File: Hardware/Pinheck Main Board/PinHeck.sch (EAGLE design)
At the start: 494 parts, among them IC2 PIC32MX795F512L-80I/PT, IC3 CD74HCT244E, IC4 CD74HCT244E, IC5 ULN2803A, J1 N/A, U1 P8X32A-Q44, U10 74HCT2G04GV,125, U11 74HC165D-Q100,118, U12 74HC165D-Q100,118, U13 CAT24M01LI-G, U14 MC74HC08ADR2G, U15 MC74HC08ADR2G, U16 MC74HC08ADR2G, U17 MC74HC08ADR2G, U18 MC74HC08ADR2G, U19 MC74HC08ADR2G, U2 DS1340Z-33+, U20 TIP107, U21 TIP107, U22 TIP107, U23 TIP107, U24 TIP107, U25 TIP107, U26 TIP107, U27 TIP107, U28 TIP102, U29 TIP102, U3 CD74HC595M96, U30 TIP102, U31 TIP102, U32 TIP102, U33 TIP102, U34 TIP102, U35 TIP102, U36 WS2801, U38 WS2801, U39 NCP1117DT33G, U4 CAT24M01LI-G, U5 CD74HC595M96, U52 CD74HC123M96, U6 TPS259251, U7 TPS259261, X1 FQ7050B-8.000, X2 9C-6.500MAAJ-T, X3 ABS25-32.768KHz-1-T

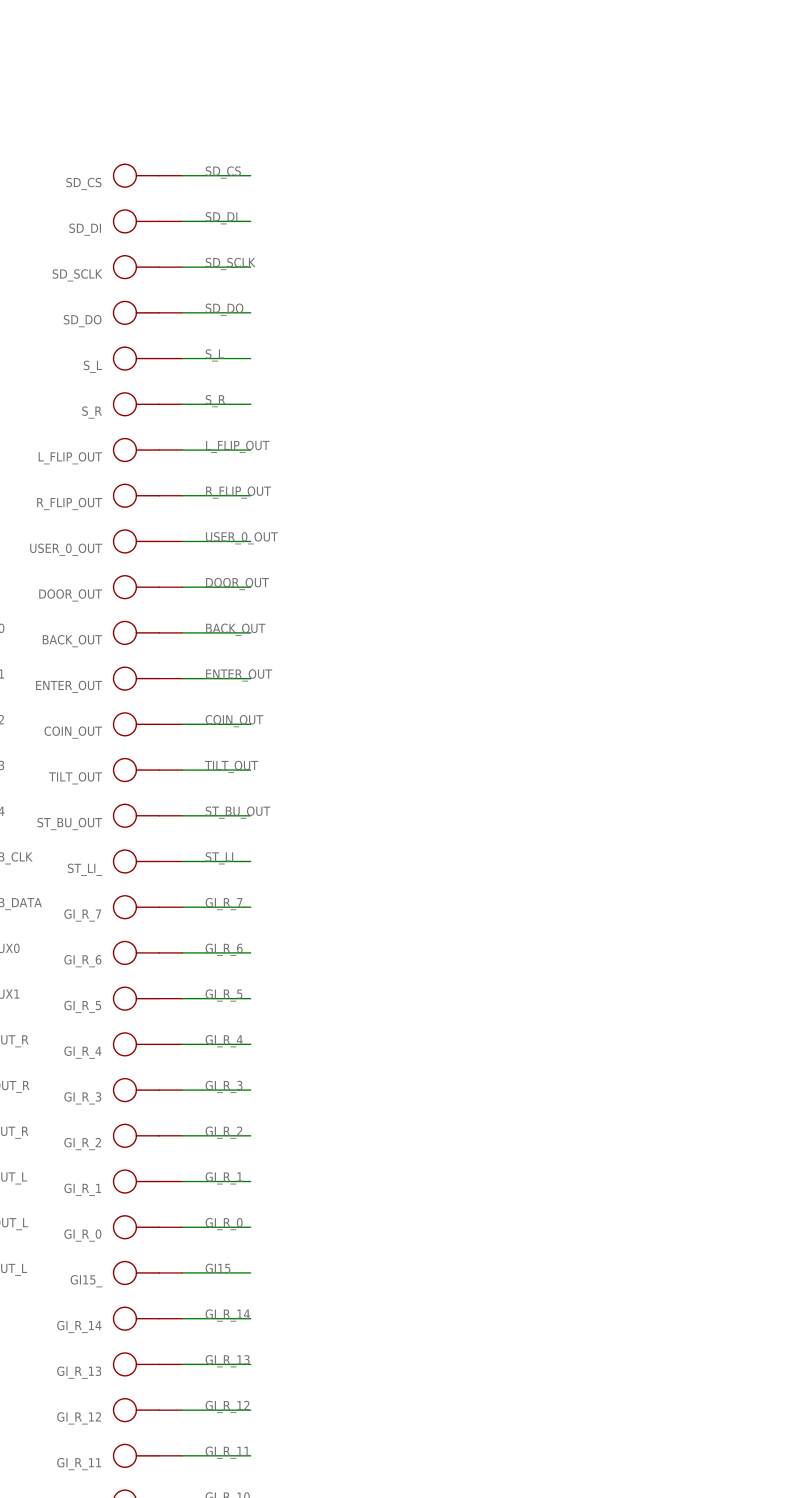
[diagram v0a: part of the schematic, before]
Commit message: finished test points.
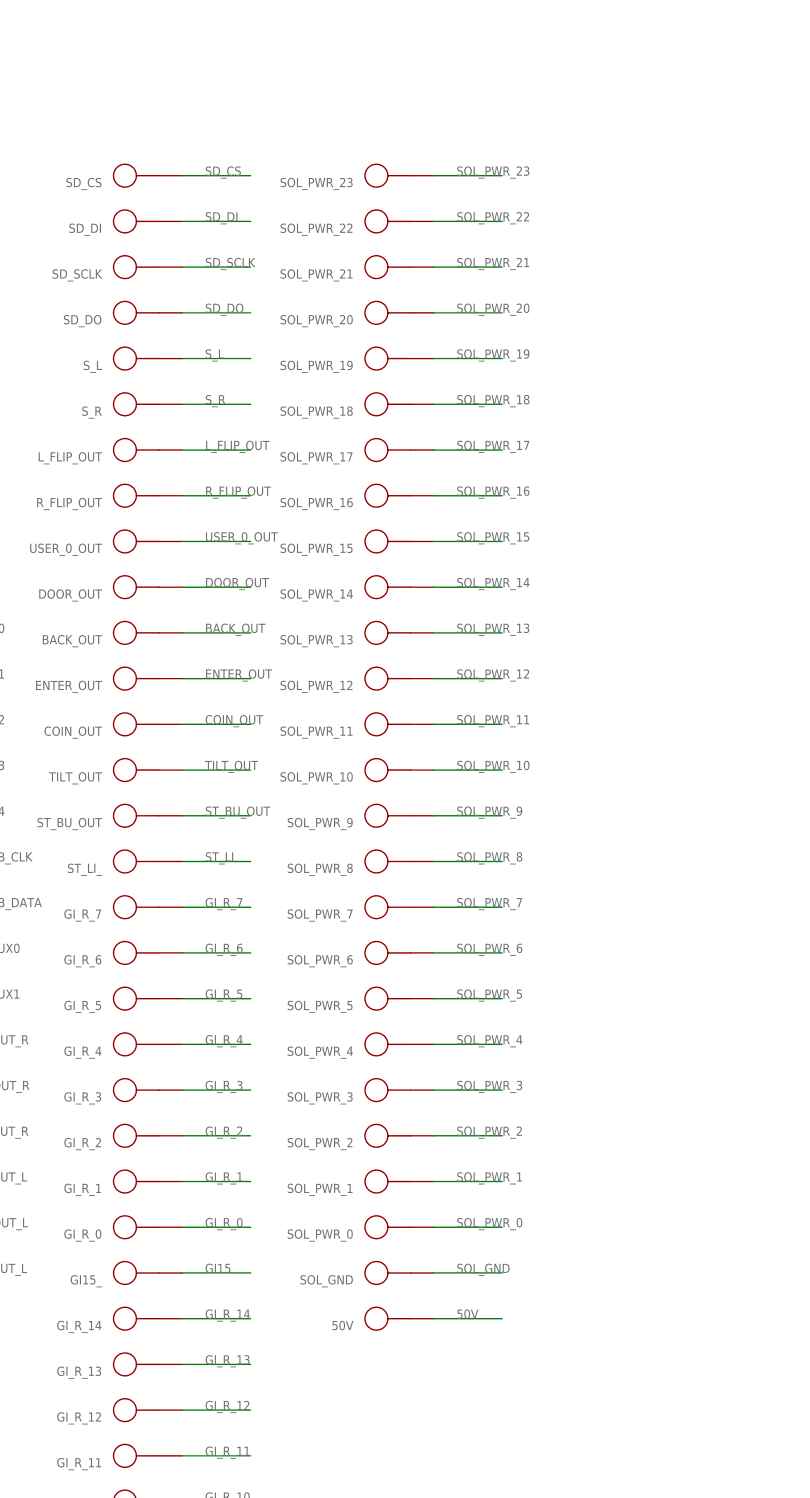
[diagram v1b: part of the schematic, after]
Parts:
- added 50V, SOL_GND, SOL_PWR_0, SOL_PWR_1, SOL_PWR_10, SOL_PWR_11, SOL_PWR_12, SOL_PWR_13, SOL_PWR_14, SOL_PWR_15, SOL_PWR_16, SOL_PWR_17, SOL_PWR_18, SOL_PWR_19, SOL_PWR_2, SOL_PWR_20, SOL_PWR_21, SOL_PWR_22, SOL_PWR_23, SOL_PWR_3, SOL_PWR_4, SOL_PWR_5, SOL_PWR_6, SOL_PWR_7, SOL_PWR_8, SOL_PWR_9: (no value), PP_Connectors:TEST_POINT_SINGLE_ROUND_100MIL
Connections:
- net 50V: now also 50V.P$1
- net SOL_GND: now also SOL_GND.P$1
- net SOL_PWR_0: now also SOL_PWR_0.P$1
- net SOL_PWR_1: now also SOL_PWR_1.P$1
- net SOL_PWR_10: now also SOL_PWR_10.P$1
- net SOL_PWR_11: now also SOL_PWR_11.P$1
- net SOL_PWR_12: now also SOL_PWR_12.P$1
- net SOL_PWR_13: now also SOL_PWR_13.P$1
- net SOL_PWR_14: now also SOL_PWR_14.P$1
- net SOL_PWR_15: now also SOL_PWR_15.P$1
- net SOL_PWR_16: now also SOL_PWR_16.P$1
- net SOL_PWR_17: now also SOL_PWR_17.P$1
- net SOL_PWR_18: now also SOL_PWR_18.P$1
- net SOL_PWR_19: now also SOL_PWR_19.P$1
- net SOL_PWR_2: now also SOL_PWR_2.P$1
- net SOL_PWR_20: now also SOL_PWR_20.P$1
- net SOL_PWR_21: now also SOL_PWR_21.P$1
- net SOL_PWR_22: now also SOL_PWR_22.P$1
- net SOL_PWR_23: now also SOL_PWR_23.P$1
- net SOL_PWR_3: now also SOL_PWR_3.P$1
- net SOL_PWR_4: now also SOL_PWR_4.P$1
- net SOL_PWR_5: now also SOL_PWR_5.P$1
- net SOL_PWR_6: now also SOL_PWR_6.P$1
- net SOL_PWR_7: now also SOL_PWR_7.P$1
- net SOL_PWR_8: now also SOL_PWR_8.P$1
- net SOL_PWR_9: now also SOL_PWR_9.P$1

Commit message: Layout complete and silkscreen almost done!
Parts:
- added SYM1: HIGH_VOLTAGE_500MIL, PP_Aesthetics:PCB_SYMBOL_HIGH_VOLTAGE_500MIL
- RGB_COM_OUT: LABEL01 (none) -> GND; LABEL02 (none) -> PROP_AUX1; LABEL03 (none) -> PROP_AUX0; LABEL04 (none) -> RGB_DATA; LABEL05 (none) -> RGB_CLK; LABEL06 (none) -> 12V; LABEL07 (none) -> 5V
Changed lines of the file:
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@@
 <grid distance="0.1" unitdist="inch" unit="inch" style="lines" multiple="1" display="no" altdistance="0.01" altunitdist="inch" altunit="inch"/>
 <layers>
-<layer number="1" name="Top" color="4" fill="1" visible="no" active="no"/>
-<layer number="2" name="Route2" color="1" fill="3" visible="no" active="no"/>
-<layer number="3" name="Route3" color="4" fill="3" visible="no" active="no"/>
-<layer number="4" name="Route4" color="1" fill="4" visible="no" active="no"/>
-<layer number="5" name="Route5" color="4" fill="4" visible="no" active="no"/>
-<layer number="6" name="Route6" color="1" fill="8" visible="no" active="no"/>
-<layer number="7" name="Route7" color="4" fill="8" visible="no" active="no"/>
-<layer number="8" name="Route8" color="1" fill="2" visible="no" active="no"/>
-<layer number="9" name="Route9" color="4" fill="2" visible="no" active="no"/>
-<layer number="10" name="Route10" color="1" fill="7" visible="no" active="no"/>
-<layer number="11" name="Route11" color="4" fill="7" visible="no" active="no"/>
-<layer number="12" name="Route12" color="1" fill="5" visible="no" active="no"/>
-<layer number="13" name="Route13" color="4" fill="5" visible="no" active="no"/>
-<layer number="14" name="Route14" color="13" fill="6" visible="no" active="no"/>
-<layer number="15" name="Route15" color="4" fill="6" visible="no" active="no"/>
-<layer number="16" name="Bottom" color="1" fill="1" visible="no" active="no"/>
-<layer number="17" name="Pads" color="2" fill="1" visible="no" active="no"/>
-<layer number="18" name="Vias" color="2" fill="1" visible="no" active="no"/>
-<layer number="19" name="Unrouted" color="6" fill="1" visible="no" active="no"/>
-<layer number="20" name="Dimension" color="15" fill="1" visible="no" active="no"/>
-<layer number="21" name="tPlace" color="7" fill="1" visible="no" active="no"/>
-<layer number="22" name="bPlace" color="7" fill="1" visible="no" active="no"/>
-<layer number="23" name="tOrigins" color="15" fill="1" visible="no" active="no"/>
-<layer number="24" name="bOrigins" color="15" fill="1" visible="no" active="no"/>
-<layer number="25" name="tNames" color="7" fill="1" visible="no" active="no"/>
-<layer number="26" name="bNames" color="7" fill="1" visible="no" active="no"/>
-<layer number="27" name="tValues" color="7" fill="1" visible="no" active="no"/>
-<layer number="28" name="bValues" color="7" fill="1" visible="no" active="no"/>
+<layer number="1" name="Top" color="4" fill="1" visible="yes" active="no"/>
+<layer number="2" name="Route2" color="1" fill="3" visible="yes" active="no"/>
+<layer number="3" name="Route3" color="4" fill="3" visible="yes" active="no"/>
+<layer number="4" name="Route4" color="1" fill="4" visible="yes" active="no"/>
+<layer number="5" name="Route5" color="4" fill="4" visible="yes" active="no"/>
+<layer number="6" name="Route6" color="1" fill="8" visible="yes" active="no"/>
+<layer number="7" name="Route7" color="4" fill="8" visible="yes" active="no"/>
+<layer number="8" name="Route8" color="1" fill="2" visible="yes" active="no"/>
+<layer number="9" name="Route9" color="4" fill="2" visible="yes" active="no"/>
+<layer number="10" name="Route10" color="1" fill="7" visible="yes" active="no"/>
+<layer number="11" name="Route11" color="4" fill="7" visible="yes" active="no"/>
+<layer number="12" name="Route12" color="1" fill="5" visible="yes" active="no"/>
+<layer number="13" name="Route13" color="4" fill="5" visible="yes" active="no"/>
+<layer number="14" name="Route14" color="13" fill="6" visible="yes" active="no"/>
+<layer number="15" name="Route15" color="4" fill="6" visible="yes" active="no"/>
+<layer number="16" name="Bottom" color="1" fill="1" visible="yes" active="no"/>
+<layer number="17" name="Pads" color="2" fill="1" visible="yes" active="no"/>
+<layer number="18" name="Vias" color="2" fill="1" visible="yes" active="no"/>
+<layer number="19" name="Unrouted" color="6" fill="1" visible="yes" active="no"/>
+<layer number="20" name="Dimension" color="15" fill="1" visible="yes" active="no"/>
+<layer number="21" name="tPlace" color="7" fill="1" visible="yes" active="no"/>
+<layer number="22" name="bPlace" color="7" fill="1" visible="yes" active="no"/>
+<layer number="23" name="tOrigins" color="15" fill="1" visible="yes" active="no"/>
+<layer number="24" name="bOrigins" color="15" fill="1" visible="yes" active="no"/>
+<layer number="25" name="tNames" color="7" fill="1" visible="yes" active="no"/>
+<layer number="26" name="bNames" color="7" fill="1" visible="yes" active="no"/>
+<layer number="27" name="tValues" color="7" fill="1" visible="yes" active="no"/>
+<layer number="28" name="bValues" color="7" fill="1" visible="yes" active="no"/>
 <layer number="29" name="tStop" color="7" fill="3" visible="no" active="no"/>
 <layer number="30" name="bStop" color="7" fill="6" visible="no" active="no"/>
@@
 <layer number="35" name="tGlue" color="7" fill="4" visible="no" active="no"/>
 <layer number="36" name="bGlue" color="7" fill="5" visible="no" active="no"/>
-<layer number="37" name="tTest" color="7" fill="1" visible="no" active="no"/>
-<layer number="38" name="bTest" color="7" fill="1" visible="no" active="no"/>
+<layer number="37" name="tTest" color="7" fill="1" visible="yes" active="no"/>
+<layer number="38" name="bTest" color="7" fill="1" visible="yes" active="no"/>
 <layer number="39" name="tKeepout" color="4" fill="11" visible="no" active="no"/>
 <layer number="40" name="bKeepout" color="1" fill="11" visible="no" active="no"/>
@@
 <layer number="44" name="Drills" color="7" fill="1" visible="no" active="no"/>
 <layer number="45" name="Holes" color="7" fill="1" visible="no" active="no"/>
-<layer number="46" name="Milling" color="3" fill="1" visible="no" active="no"/>
-<layer number="47" name="Measures" color="7" fill="1" visible="no" active="no"/>
-<layer number="48" name="Document" color="7" fill="1" visible="no" active="no"/>
-<layer number="49" name="Reference" color="7" fill="1" visible="no" active="no"/>
-<layer number="50" name="dxf" color="7" fill="1" visible="no" active="no"/>
-<layer number="51" name="tDocu" color="7" fill="1" visible="no" active="no"/>
-<layer number="52" name="bDocu" color="7" fill="1" visible="no" active="no"/>
-<layer number="53" name="tGND_GNDA" color="7" fill="9" visible="no" active="no"/>
-<layer number="54" name="bGND_GNDA" color="1" fill="9" visible="no" active="no"/>
-<layer number="56" name="wert" color="7" fill="1" visible="no" active="no"/>
+<layer number="46" name="Milling" color="3" fill="1" visible="yes" active="no"/>
+<layer number="47" name="Measures" color="7" fill="1" visible="yes" active="no"/>
+<layer number="48" name="Document" color="7" fill="1" visible="yes" active="no"/>
+<layer number="49" name="Reference" color="7" fill="1" visible="yes" active="no"/>
+<layer number="50" name="dxf" color="7" fill="1" visible="yes" active="no"/>
+<layer number="51" name="tDocu" color="7" fill="1" visible="yes" active="no"/>
+<layer number="52" name="bDocu" color="7" fill="1" visible="yes" active="no"/>
+<layer number="53" name="tGND_GNDA" color="7" fill="9" visible="yes" active="no"/>
+<layer number="54" name="bGND_GNDA" color="1" fill="9" visible="yes" active="no"/>
+<layer number="56" name="wert" color="7" fill="1" visible="yes" active="no"/>
 <layer number="91" name="Nets" color="2" fill="1" visible="yes" active="yes"/>
 <layer number="92" name="Busses" color="1" fill="1" visible="yes" active="yes"/>
@@
 <part name="C55" library="PP_Passives" deviceset="CAPACITOR_NON_POLAR" device="_0805" value=".1uF"/>
 <part name="SHAKER" library="PP_Connectors" deviceset="CON_01X02" device="_26-64-4020" value="26-64-4020"/>
-<part name="RGB_COM_OUT" library="PP_Connectors" deviceset="CON_01X07" device="_26-64-4080(KEYPIN2)" value="26-64-4080"/>
+<part name="RGB_COM_OUT" library="PP_Connectors" deviceset="CON_01X07" device="_26-64-4080(KEYPIN2)" value="26-64-4080">
+<attribute name="LABEL01" value="GND"/>
+<attribute name="LABEL02" value="PROP_AUX1"/>
+<attribute name="LABEL03" value="PROP_AUX0"/>
+<attribute name="LABEL04" value="RGB_DATA"/>
+<attribute name="LABEL05" value="RGB_CLK"/>
+<attribute name="LABEL06" value="12V"/>
+<attribute name="LABEL07" value="5V"/>
+</part>
 <part name="H3" library="PP_Connectors" deviceset="MOUNT_HOLE" device="150MIL"/>
 <part name="H4" library="PP_Connectors" deviceset="MOUNT_HOLE" device="150MIL"/>
@@
 <part name="SOL_GND" library="PP_Connectors" deviceset="TEST_POINT_SINGLE" device="_ROUND_100MIL"/>
 <part name="50V" library="PP_Connectors" deviceset="TEST_POINT_SINGLE" device="_ROUND_100MIL"/>
+<part name="SYM1" library="PP_Aesthetics" deviceset="PCB_SYMBOL" device="_HIGH_VOLTAGE_500MIL" value="HIGH_VOLTAGE_500MIL"/>
 </parts>
 <sheets>
@@
 <instance part="SOL_GND" gate="G$1" x="-43.18" y="-91.44" rot="R180"/>
 <instance part="50V" gate="G$1" x="-43.18" y="-96.52" rot="R180"/>
+<instance part="SYM1" gate="G$1" x="-99.06" y="187.96"/>
 </instances>
 <busses>
